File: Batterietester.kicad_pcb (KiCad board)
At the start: 2 copper layers, 67 x 53 mm, 23 parts, among them J1 CONN_01X02, J2 CONN_01X02, J3 CONN_01X02, J4 CONN_01X02, SW1 SW_Push, SW2 SW_Push, U1 LM3914

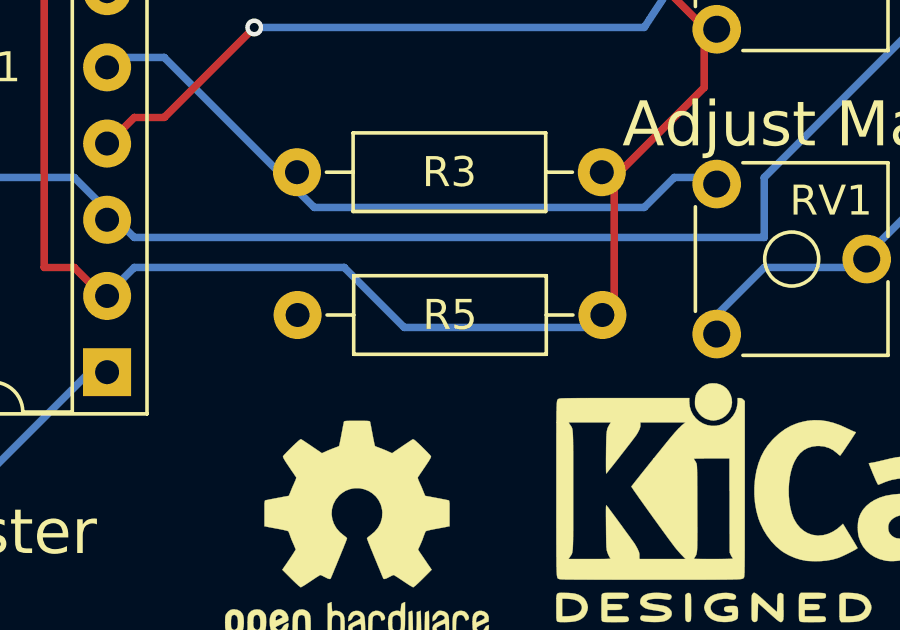
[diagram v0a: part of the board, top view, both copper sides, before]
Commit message: delete needless R5
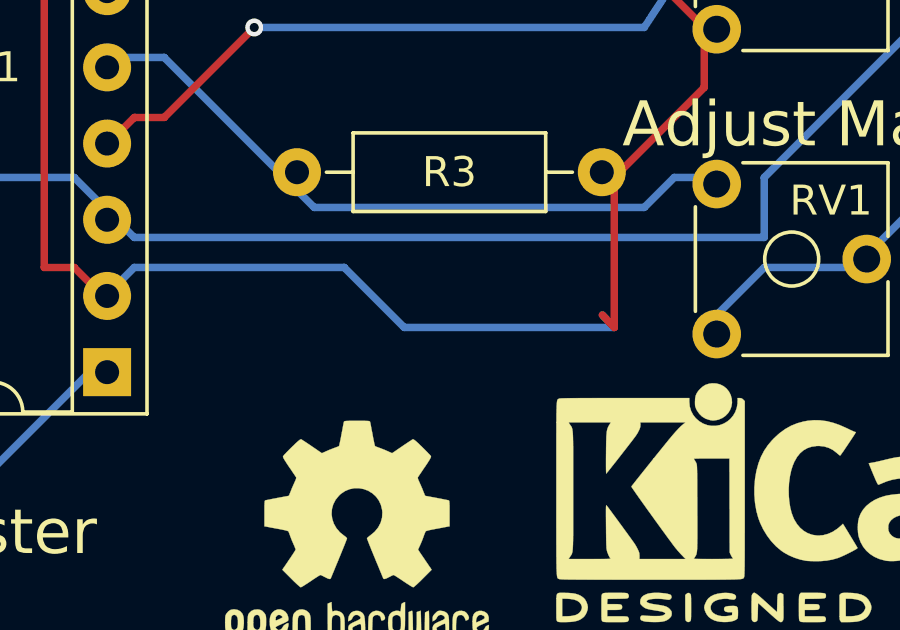
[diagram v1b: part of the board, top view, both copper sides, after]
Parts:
- removed R5: 10k, Resistors_ThroughHole:R_Axial_DIN0207_L6.3mm_D2.5mm_P10.16mm_Horizontal
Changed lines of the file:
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@@
 (kicad_pcb (version 4) (host pcbnew 4.0.6+dfsg1-1)
   (general
-    (links 53)
+    (links 52)
     (no_connects 0)
-    (area 80 60 180 133)
+    (area 80.575001 60.125 180.275 132.525001)
     (thickness 1.6)
     (drawings 36)
     (tracks 308)
     (zones 0)
-    (modules 23)
+    (modules 22)
     (nets 21)
   )
@@
     (35 F.Paste user)
     (36 B.SilkS user)
-    (37 F.SilkS user hide)
+    (37 F.SilkS user)
     (38 B.Mask user)
     (39 F.Mask user)
@@
       (at (xyz 0 0 0))
       (scale (xyz 0.393701 0.393701 0.393701))
-      (rotate (xyz 0 0 0))
-    )
-  )
-  (module Resistors_ThroughHole:R_Axial_DIN0207_L6.3mm_D2.5mm_P10.16mm_Horizontal (layer F.Cu)
-    (at 131.445 108.585)
-    (descr "Resistor, Axial_DIN0207 series, Axial, Horizontal, pin pitch=10.16mm, 0.25W = 1/4W, length*diameter=6.3*2.5mm^2, http://cdn-reichelt.de/documents/datenblatt/B400/1_4W%23YAG.pdf")
-    (tags "Resistor Axial_DIN0207 series Axial Horizontal pin pitch 10.16mm 0.25W = 1/4W length 6.3mm diameter 2.5mm")
-    (fp_text reference R5 (at 5.08 0) (layer F.SilkS)
-      (effects (font (size 1 1) (thickness 0.15)))
-    )
-    (fp_text value 10k (at 5.08 2.31) (layer F.Fab)
-      (effects (font (size 1 1) (thickness 0.15)))
-    )
-    (fp_line (start 1.93 -1.25) (end 1.93 1.25) (layer F.Fab) (width 0.1))
-    (fp_line (start 1.93 1.25) (end 8.23 1.25) (layer F.Fab) (width 0.1))
-    (fp_line (start 8.23 1.25) (end 8.23 -1.25) (layer F.Fab) (width 0.1))
-    (fp_line (start 8.23 -1.25) (end 1.93 -1.25) (layer F.Fab) (width 0.1))
-    (fp_line (start 0 0) (end 1.93 0) (layer F.Fab) (width 0.1))
-    (fp_line (start 10.16 0) (end 8.23 0) (layer F.Fab) (width 0.1))
-    (fp_line (start 1.87 -1.31) (end 1.87 1.31) (layer F.SilkS) (width 0.12))
-    (fp_line (start 1.87 1.31) (end 8.29 1.31) (layer F.SilkS) (width 0.12))
-    (fp_line (start 8.29 1.31) (end 8.29 -1.31) (layer F.SilkS) (width 0.12))
-    (fp_line (start 8.29 -1.31) (end 1.87 -1.31) (layer F.SilkS) (width 0.12))
-    (fp_line (start 0.98 0) (end 1.87 0) (layer F.SilkS) (width 0.12))
-    (fp_line (start 9.18 0) (end 8.29 0) (layer F.SilkS) (width 0.12))
-    (fp_line (start -1.05 -1.6) (end -1.05 1.6) (layer F.CrtYd) (width 0.05))
-    (fp_line (start -1.05 1.6) (end 11.25 1.6) (layer F.CrtYd) (width 0.05))
-    (fp_line (start 11.25 1.6) (end 11.25 -1.6) (layer F.CrtYd) (width 0.05))
-    (fp_line (start 11.25 -1.6) (end -1.05 -1.6) (layer F.CrtYd) (width 0.05))
-    (pad 1 thru_hole circle (at 0 0) (size 1.6 1.6) (drill 0.8) (layers *.Cu *.Mask))
-    (pad 2 thru_hole oval (at 10.16 0) (size 1.6 1.6) (drill 0.8) (layers *.Cu *.Mask)
-      (net 1 GND))
-    (model ${KISYS3DMOD}/Resistors_THT.3dshapes/R_Axial_DIN0207_L6.3mm_D2.5mm_P10.16mm_Horizontal.wrl
-      (at (xyz 0 0 0))
-      (scale (xyz 0.393701 0.393701 0.393701))

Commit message: layout changes
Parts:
- D1: footprint LEDs:LED_D5.0mm -> LEDs:LED_D3.0mm
- RV1, RV2: footprint Potentiometers:Potentiometer_Trimmer_ACP_CA6v_Horizontal -> Potentiometers:Potentiometer_Trimmer_Copal_CT-6EP
- SW1, SW2: footprint Buttons_Switches_ThroughHole:SW_PUSH_6mm_h5mm -> Buttons_Switches_ThroughHole:SW_PUSH_6mm
- moved C1 28.5 mm to (129.4, 107.8), turned to 90 degrees
- moved RV1 5.33 mm to (148.4, 104.8)
- moved RV2 5.20 mm to (148.4, 94.8)
- moved R3 5.00 mm to (131.4, 98.8)
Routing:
- net GND: track 121.4 -> 0.00 mm
- net 9V: track 194.9 -> 149.4 mm, vias 2 -> 0
- net Net-(BAR1-Pad16): track 14.5 -> 46.4 mm, vias 0 -> 2
- net Net-(BAR1-Pad15): track 45.8 -> 17.0 mm, vias 2 -> 0
- net Net-(BAR1-Pad17): track 25.9 -> 39.0 mm, vias 0 -> 1
- net Net-(BAR1-Pad18): track 31.6 -> 19.8 mm, vias 1 -> 0
- net Net-(BAR1-Pad14): track 41.7 -> 34.5 mm
- net Net-(R3-Pad1): track 24.2 -> 29.7 mm, vias 0 -> 1
- net Net-(J4-Pad1): track 30.8 -> 25.3 mm, vias 1 -> 0
- net Net-(R4-Pad1): track 25.6 -> 30.3 mm
- net Sig: track 20.6 -> 17.2 mm
- net Net-(BAR1-Pad19): track 15.5 -> 17.1 mm
- net Net-(BAR1-Pad12): track 27.9 -> 28.7 mm, vias 0 -> 1
- net Net-(BAR1-Pad20): vias 0 -> 1
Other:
- board text added: "Rev 2"
- board text removed: "Rev 1"

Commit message: change layout
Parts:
- moved REF*** 1.00 mm to (133.4, 114.8)
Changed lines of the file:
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@@
     (links 52)
     (no_connects 0)
-    (area 80 60 180 133)
+    (area 98.349999 70.749999 165.500001 123.900001)
     (thickness 1.6)
     (drawings 36)
@@
     (descr "CP, Radial series, Radial, pin pitch=1.50mm, , diameter=4mm, Electrolytic Capacitor")
     (tags "CP Radial series Radial pin pitch 1.50mm  diameter 4mm Electrolytic Capacitor")
-    (fp_text reference C1 (at -0.635 0 180) (layer F.SilkS)
+    (fp_text reference C1 (at -3 0 180) (layer F.SilkS)
       (effects (font (size 1 1) (thickness 0.15)))
     )
@@
   )
   (module Symbols:OSHW-Logo2_9.8x8mm_SilkScreen (layer F.Cu)
-    (at 133.425 115.825)
+    (at 133.425 114.825)
     (descr "Open Source Hardware Symbol")
     (tags "Logo Symbol OSHW")

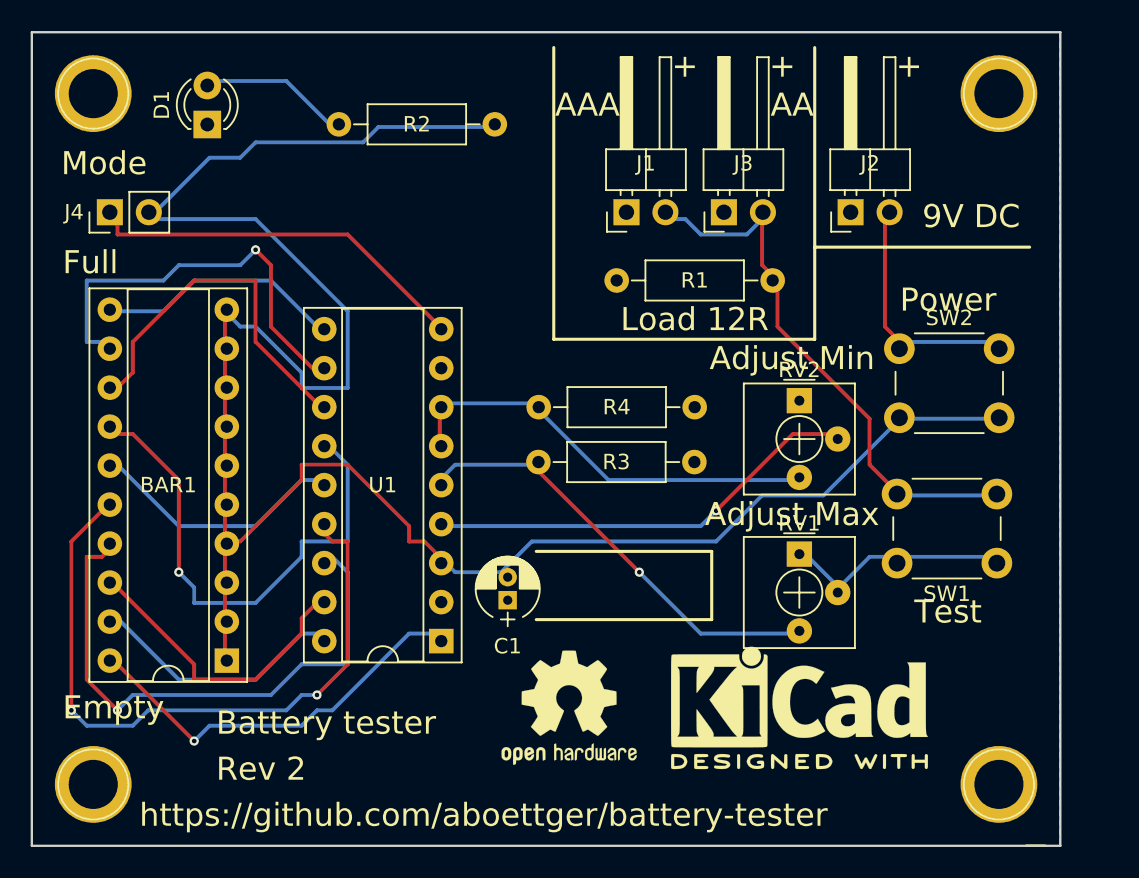
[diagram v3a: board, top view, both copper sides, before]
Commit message: redesign
- add terminal blocks
- use freerouter
- fix some ref errors
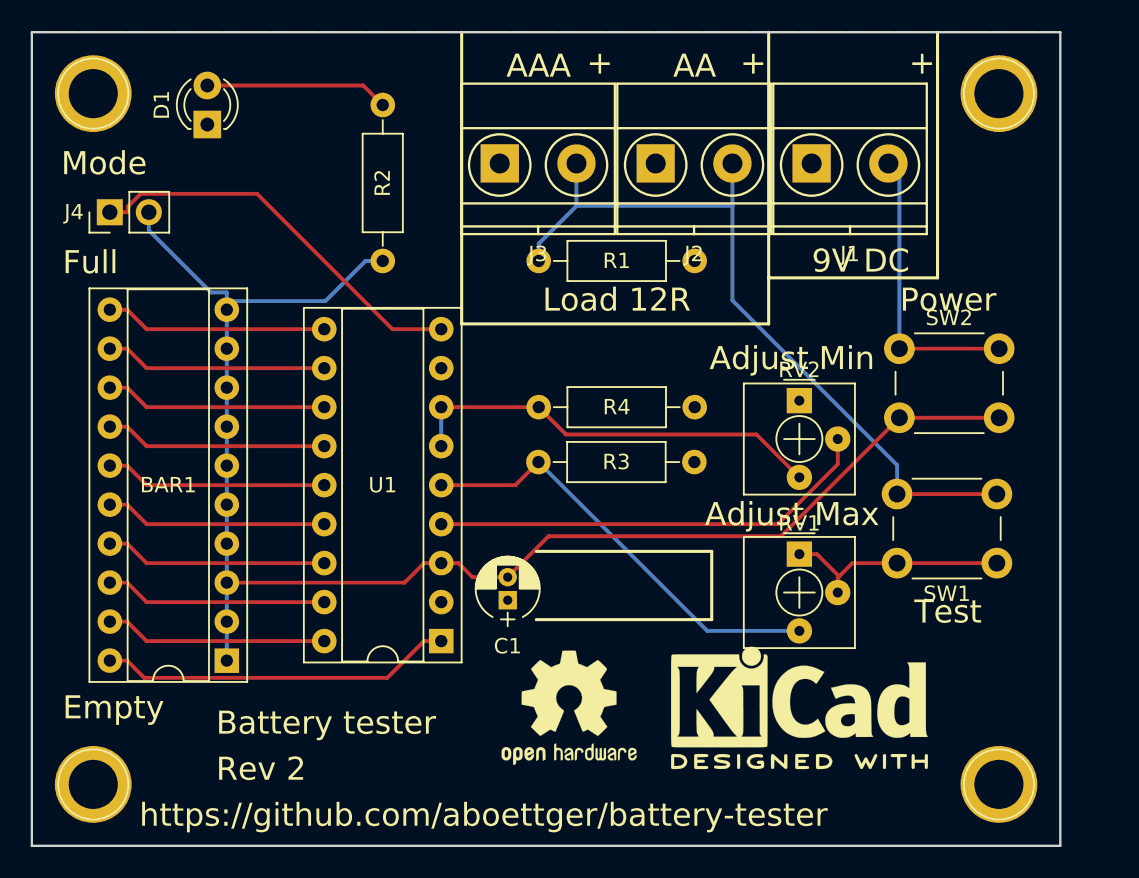
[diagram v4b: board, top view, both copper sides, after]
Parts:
- J1, J2, J3: value CONN_01X02 -> Screw_Terminal_1x02; footprint Pin_Headers:Pin_Header_Angled_1x02_Pitch2.54mm -> TerminalBlock_Phoenix:TerminalBlock_Phoenix_MKDS1.5-2pol
- moved J3 14.9 mm to (128.9, 79.4), turned to 0 degrees
- moved J2 13.1 mm to (139.1, 79.4), turned to 0 degrees
- moved J1 12.5 mm to (149.2, 79.4), turned to 0 degrees
- moved R1 5.24 mm to (141.6, 85.7)
- moved R2 3.13 mm to (121.3, 75.6), turned to 270 degrees
- renumbered REF** to H1, REF** to H2, REF** to H3, REF** to H4, REF*** to kicad, REF*** to openhardware
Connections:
- J1 pad 2: SW_L -> Net-(J1-Pad2)
- J2 pad 2: Net-(J2-Pad2) -> SW_L
- R1 pad 1: SW_L -> GND
- R1 pad 2: GND -> SW_L
- SW2 pad 1: Net-(J2-Pad2) -> Net-(J1-Pad2)
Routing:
- net 9V: track 149.4 -> 98.7 mm
- net Net-(BAR1-Pad16): track 46.4 -> 14.5 mm, vias 2 -> 0
- net Net-(BAR1-Pad17): track 39.0 -> 14.5 mm, vias 1 -> 0
- net Net-(BAR1-Pad14): track 34.5 -> 14.5 mm, vias 1 -> 0
- net Net-(J1-Pad2): track 0.00 -> 18.9 mm
- net Net-(J2-Pad2): track 16.5 -> 0.00 mm
- net Net-(BAR1-Pad12): track 28.7 -> 14.5 mm, vias 1 -> 0
- net SW_L: track 37.4 -> 50.0 mm
- net Net-(BAR1-Pad13): track 23.8 -> 14.5 mm
- net Net-(BAR1-Pad18): track 19.8 -> 14.5 mm
- net Net-(BAR1-Pad20): track 27.0 -> 23.0 mm, vias 1 -> 0
- net Net-(BAR1-Pad19): track 17.1 -> 14.5 mm
- net Net-(R4-Pad1): track 30.3 -> 27.8 mm
- net Net-(BAR1-Pad15): track 17.0 -> 14.5 mm
- net Sig: track 17.2 -> 14.9 mm
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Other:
- outline, holes or cut-outs redrawn

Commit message: swap positions RV1, RV2
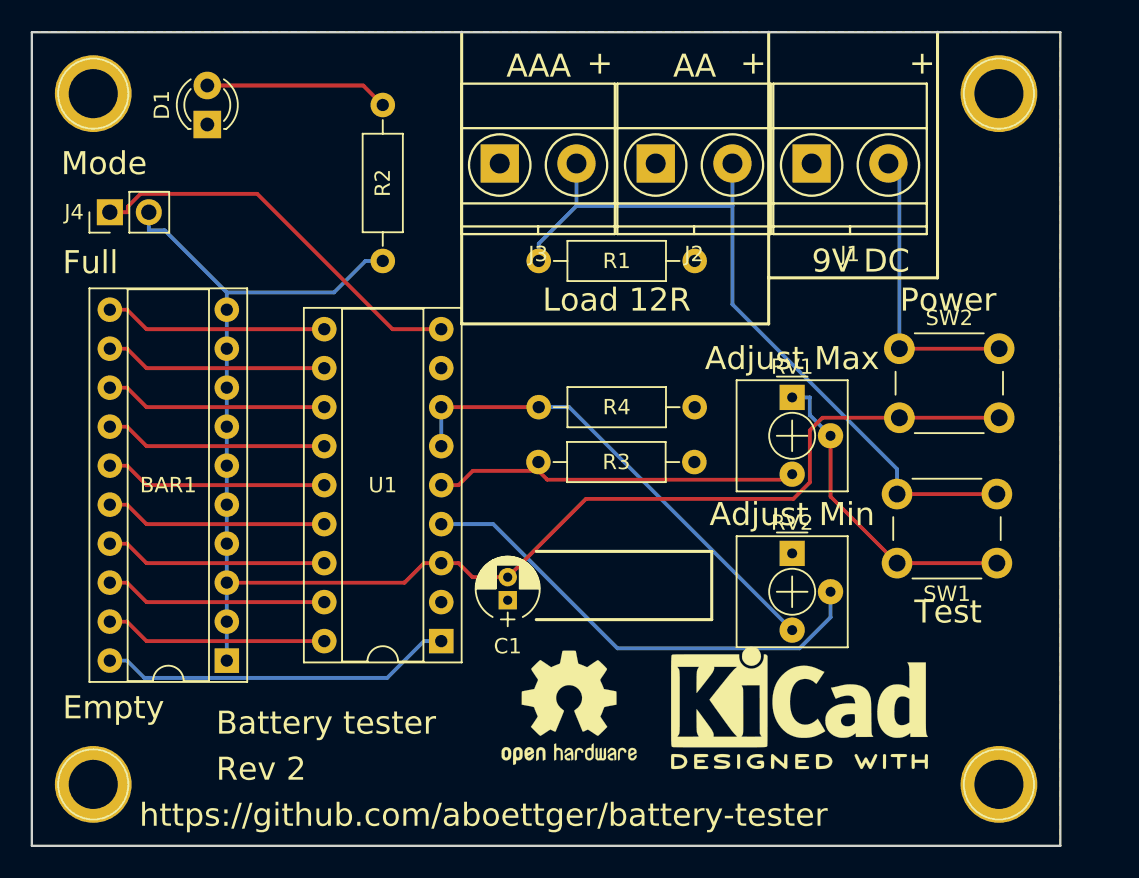
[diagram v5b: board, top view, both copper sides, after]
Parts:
- moved RV1 10.2 mm to (148.0, 94.6)
- moved RV2 9.96 mm to (148.0, 104.8)
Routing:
- net Sig: track 14.9 -> 20.8 mm
- net Net-(R3-Pad1): track 28.5 -> 24.2 mm
- net Net-(R4-Pad1): track 27.8 -> 31.4 mm
- net Pin4: track 29.1 -> 31.2 mm
- net 9V: track 98.7 -> 100.4 mm

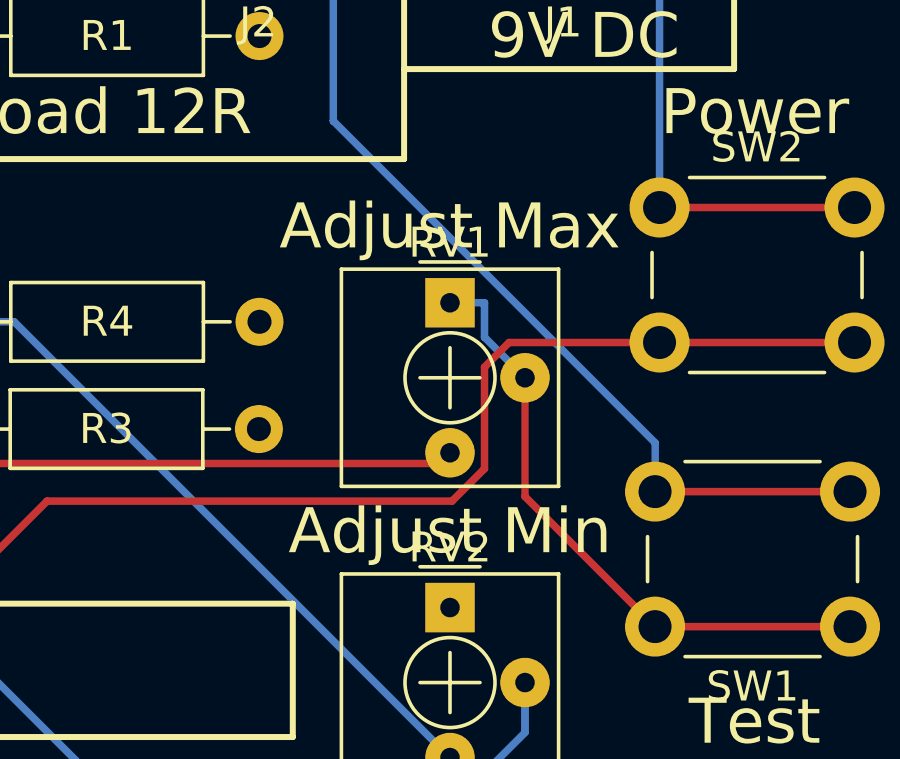
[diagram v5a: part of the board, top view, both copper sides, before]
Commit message: wording
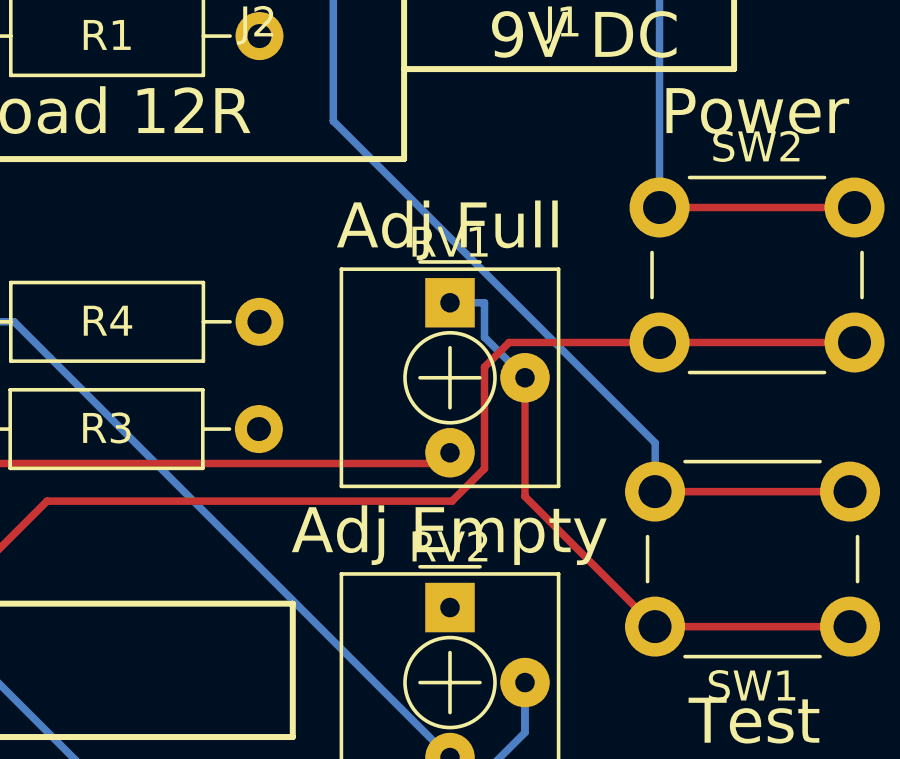
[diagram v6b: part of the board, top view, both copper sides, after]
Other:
- board text added: "Adj Empty"
- board text added: "Adj Full"
- board text removed: "Adjust Max"
- board text removed: "Adjust Min"
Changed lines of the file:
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@@
     (links 52)
     (no_connects 0)
-    (area 98.349999 70.749999 165.500001 123.900001)
+    (area 80.575001 60.125 180.275 132.525001)
     (thickness 1.6)
     (drawings 35)
@@
     (effects (font (size 1.5 1.5) (thickness 0.3)) (justify mirror))
   )
-  (gr_text "Adjust Max" (at 147.955 92.075) (layer F.SilkS)
+  (gr_text "Adj Full" (at 147.955 92.075) (layer F.SilkS)
     (effects (font (size 1.5 1.5) (thickness 0.3)))
   )
-  (gr_text "Adjust Min" (at 147.955 102.235) (layer F.SilkS)
+  (gr_text "Adj Empty" (at 147.955 102.235) (layer F.SilkS)
     (effects (font (size 1.5 1.5) (thickness 0.3)))
   )
